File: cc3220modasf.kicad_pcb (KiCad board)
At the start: 4 copper layers, 48.5 x 56.8 mm, 90 parts, among them J1 Conn_02x05_Odd_Even, J10 Conn_01x02, J11 Conn_02x04_Odd_Even, J13 Conn_02x05_Counter_Clockwise, J14 Conn_01x02, J15 Conn_01x02, J2 Conn_02x05_Odd_Even, J22 Conn_02x04_Odd_Even, J26 Conn_01x03, J3 Conn_01x06, J5 Conn_01x03, J6 Conn_01x03, Q4 BSS138, Q5 TP0610T, Q6 BSS138, Q7 BSS138, SW2 SW_DIP_x01, U10 TMP006AIYZFR, U7 OPA4340UA, U9 CC3220MODASF12MONR

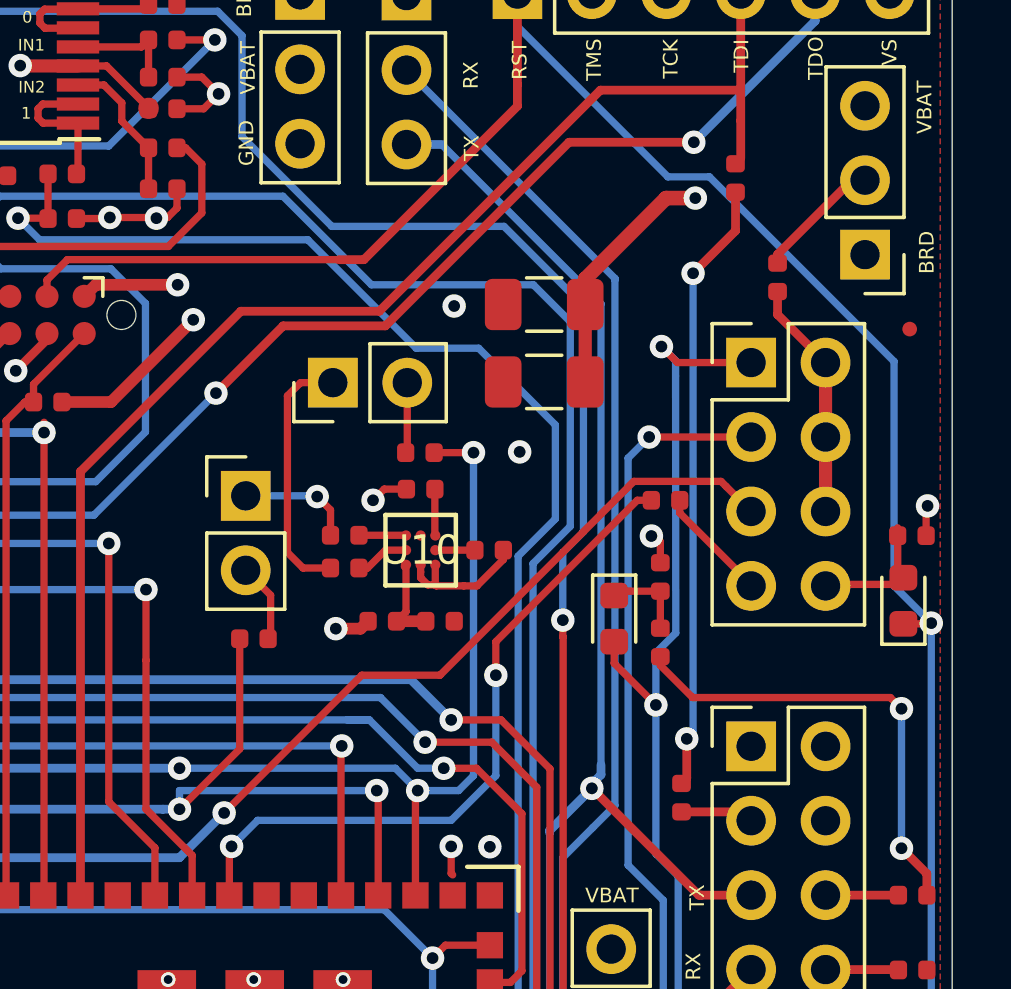
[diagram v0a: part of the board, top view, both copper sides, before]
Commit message: Changed U10 to TMP116AIDRVR. Added new sybmol/footprint bom, pos files and README into repo.
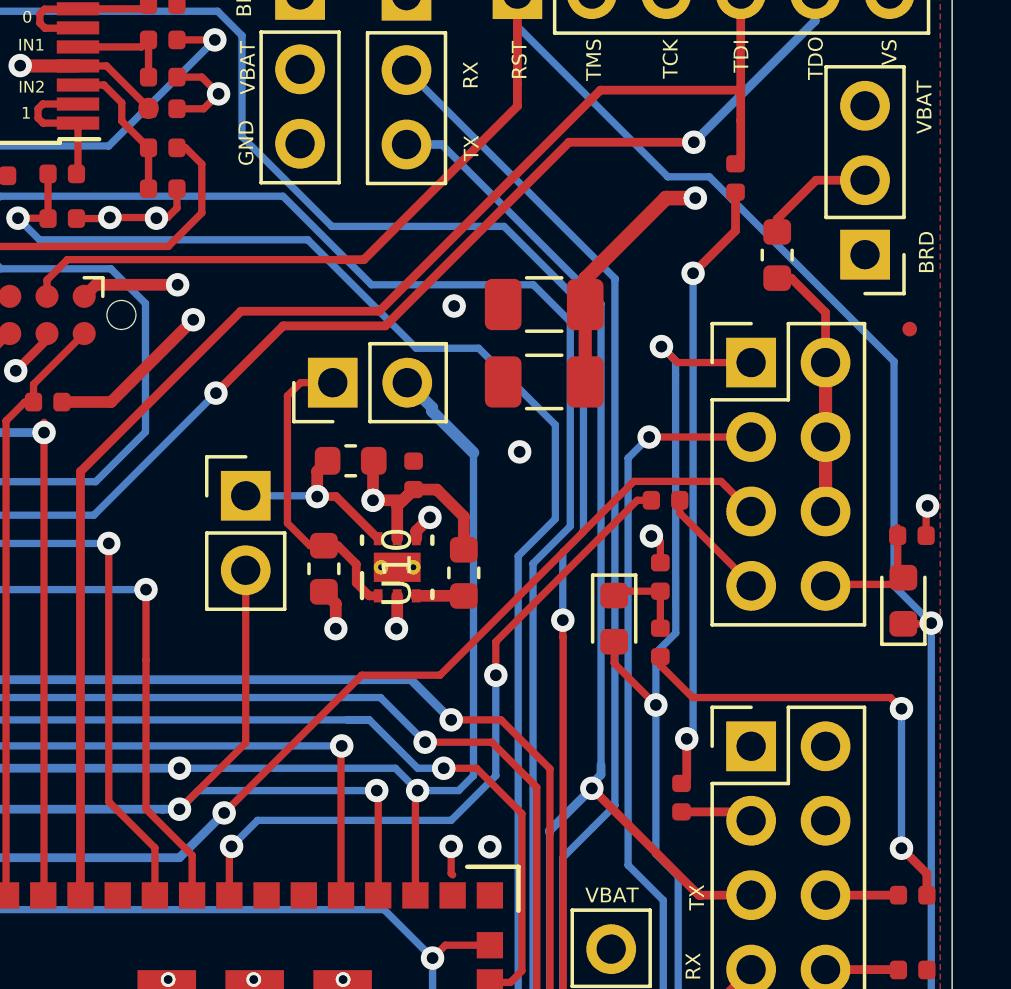
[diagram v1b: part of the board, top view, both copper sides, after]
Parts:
- removed R114, R119, R121, R126, R127, R132, R133: 0, Resistor_SMD:R_0402_1005Metric
- added R116: 4k87, Resistor_SMD:R_0603_1608Metric, F.Cu at (104.1, 81.1)
- added R117: 4k87, Resistor_SMD:R_0603_1608Metric, F.Cu at (103.2, 84.8)
- added R118: 4k87, Resistor_SMD:R_0603_1608Metric, F.Cu at (108.0, 84.9)
- D10: value LED -> RED LED
- D8: value LED -> GREEN LED
- D9: value LED -> YELLOW LED
- Q5: value TP0610T -> FDN358P
- R107: value 270 -> 270R; footprint Resistor_SMD:R_0402_1005Metric -> Resistor_SMD:R_0603_1608Metric
- R145, R146, R147: value 270 -> 270R
- R84, R87, R92, R93: value 470 -> 470R
- U10: value TMP006AIYZFR -> TMP116AIDRVR; footprint TMP006AIYZFR:TMP006AIYZFR -> TMP116:TMP116AIDRVR
- moved C35 5.06 mm to (106.3, 81.6), turned to 90 degrees
- moved U10 0.99 mm to (105.7, 84.7), turned to 90 degrees
- moved R107 0.76 mm to (118.7, 74.1)
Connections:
- C35 pad 1: GND -> /VCC_BRD
- C35 pad 2: Net-(C35-Pad2) -> GND
- J14 pad 2: Net-(J14-Pad2) -> /P01_GPIO_10
- J15 pad 2: Net-(J15-Pad2) -> /P02_GPIO_11
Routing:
- net /VCC_BRD: track 37.3 -> 44.3 mm
- net Net-(C35-Pad2): track 3.15 -> 0.00 mm
- net Net-(J15-Pad2): track 2.72 -> 0.00 mm
- net GND: track 27.2 -> 24.5 mm, vias 53 -> 55
- net /SENS_I2C_SDA: track 3.99 -> 6.53 mm
- net Net-(J14-Pad2): track 2.41 -> 0.00 mm
- net /P02_GPIO_11: track 56.7 -> 58.7 mm
- net /P01_GPIO_10: track 66.4 -> 68.4 mm, vias 4 -> 3
- net Net-(R132-Pad1): track 1.86 -> 0.00 mm
- net /SENS_I2C_SCL: track 8.77 -> 10.6 mm
- net Net-(R118-Pad1): track 0.00 -> 1.62 mm
- net Net-(R133-Pad2): track 1.61 -> 0.00 mm
- net Net-(R119-Pad1): track 1.59 -> 0.00 mm
- net Net-(R126-Pad2): track 1.35 -> 0.00 mm
- net Net-(J22-Pad2): track 8.18 -> 8.92 mm
